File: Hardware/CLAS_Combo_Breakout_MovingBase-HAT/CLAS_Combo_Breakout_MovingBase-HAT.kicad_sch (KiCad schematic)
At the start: 86 parts, among them J1 USB_C_Receptacle_USB2.0, J2 ZED, J3 NEO, J4 USB_C_Receptacle_USB2.0, J5 Conn_Coaxial, Q1 DSS20200, U1 USBLC6-2P6, U2 ZED-F9P, U3 NEO-D9C-00B, U4 USBLC6-2P6, U5 NJU77251F, U6 AP2112K-3.3, U7 NT1191GEAE3S, U8 F2933NBGP, U9 PD0922J5050S2HF

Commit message: ISP4520周辺回路を設計中
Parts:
- removed ANT1: GGBLA.125.A, GGBLA.125.A:GGBLA.125.A, symbol GGBLA.125.A:GGBLA.125.A
- removed BT1: MS421R, Battery_extlib:MS421R, symbol Device:Battery_Cell
- removed C1, C10, C5, C6: 1u, Capacitor_SMD:C_0603_1608Metric, symbol Device:C_Small
- removed C11, C14: 47p, Capacitor_SMD:C_0402_1005Metric, symbol Device:C_Small
- removed C12: 1000p, Capacitor_SMD:C_0603_1608Metric, symbol Device:C_Small
- removed C13: 3.9p, Capacitor_SMD:C_0402_1005Metric, symbol Device:C_Small
- removed C15, C2, C3, C4: 0.1u, Capacitor_SMD:C_0603_1608Metric, symbol Device:C_Small
- removed C16: 1.2p, Capacitor_SMD:C_0402_1005Metric, symbol Device:C_Small
- removed C9: DNF, Capacitor_SMD:C_0402_1005Metric, symbol Device:C_Small
- removed D10: PESD0402-140, Diode_SMD:D_0402_1005Metric, symbol Device:D_TVS
- removed D3: EXTANT, LED_SMD:LED_0603_1608Metric, symbol Device:LED_Small
- removed D7: CUHS20S30, CUHS20S30:CUHS20S30, symbol Device:D_Schottky_Small
- removed D8: BAS19, Package_TO_SOT_SMD:SOT-23, symbol Diode:BAS19
- removed D9: BAT54W, Package_TO_SOT_SMD:SOT-23, symbol Diode:BAT54W
- removed J4: USB_C_Receptacle_USB2.0, Connector_USB_extlib:USB_C_Receptacle_5077CR-16-SMC2-BK-TR, symbol Connector:USB_C_Receptacle_USB2.0
- removed J5: Conn_Coaxial, Connector_Coaxial_extlib:0734152063, symbol Connector:Conn_Coaxial
- removed L1: LQW18ANR12G8ZD, LQW18ANR12G8ZD:LQW18ANR12G8ZD, symbol Device:L_Small
- removed L2: LQW15AN9N5G00D, LQW15AN9N5G00D:LQW15AN9N5G00D, symbol Device:L_Small
- removed Q1: DSS20200, Package_TO_SOT_SMD:SOT-23, symbol DSS20200L-7:DSS20200L-7
- removed R1, R11, R12, R2, R3, R4, R5, R6, R7: 33, Resistor_SMD:R_0603_1608Metric, symbol Device:R_Small
- removed R10, R13, R14, R16: 27, Resistor_SMD:R_0603_1608Metric, symbol Device:R_Small
- removed R15, R17: 5.1k, Resistor_SMD:R_0603_1608Metric, symbol Device:R_Small
- removed R20: 1k, Resistor_SMD:R_0603_1608Metric, symbol Device:R_Small
- removed R24: 68, Resistor_SMD:R_0402_1005Metric, symbol Device:R_Small
- removed R25: 3, Resistor_SMD:R_0603_1608Metric, symbol Device:R_Small
- removed R26: 22k, Resistor_SMD:R_0402_1005Metric, symbol Device:R_Small
- removed R27: 3.3k, Resistor_SMD:R_0603_1608Metric, symbol Device:R_Small
- removed R28: 1.5k, Resistor_SMD:R_0402_1005Metric, symbol Device:R_Small
- removed R29, R30: 100, Resistor_SMD:R_0402_1005Metric, symbol Device:R_Small
- removed R31, R33, R34: 0, Resistor_SMD:R_0402_1005Metric, symbol Device:R_Small
- removed R32: DNF, Resistor_SMD:R_0402_1005Metric, symbol Device:R_Small
- removed TP1: SAFEBOOT_ZED, TestPoint:TestPoint_Pad_D1.0mm, symbol Connector:TestPoint
- removed TP2: SAFEBOOT_NEO, TestPoint:TestPoint_Pad_D1.0mm, symbol Connector:TestPoint
- removed U2: ZED-F9P, RF_GPS:ublox_ZED, symbol RF_GPS:ZED-F9P
- removed U3: NEO-D9C-00B, NEO-D9:NEO-D9, symbol NEO-D9:NEO-D9C-00B
- removed U4: USBLC6-2P6, Package_TO_SOT_SMD:SOT-666, symbol Power_Protection:USBLC6-2P6
- removed U5: NJU77251F, Package_TO_SOT_SMD:SOT-23-5, symbol Comparator:LMV331
- removed U7: NT1191GEAE3S, NT1191GEAE3S:NT1191GEAE3S, symbol NT1191GEAE3S:NT1191GEAE3S
- removed U8: F2933NBGP, F2933NBGP:F2933NBGP, symbol F2933NBGP:F2933NBGP
- removed U9: PD0922J5050S2HF, PD0922J5050S2HF:PD0922J5050S2HF_ANA, symbol PD0922J5050S2HF:PD0922J5050S2HF
- added C?: 1u, symbol Device:C_Small
- added C? (x2): 0.1u, symbol Device:C_Small
- added D?: CUHS20S30, CUHS20S30:CUHS20S30, symbol Device:D_Schottky_Small
- added R?: 10k, symbol Device:R_Small
- added SW?: SW_Push, symbol Switch:SW_Push
- added U?: ISP4520-AS, symbol ISP4520-AS:ISP4520-AS
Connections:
- net +3.3V: now also C?.1, C?.1, D?.1 (K), R?.1, U?.15 (VDD)
- net GND: now also C?.2, C?.2, SW?.2, U?.1 (GND), U?.14 (GND), U?.21 (GND), U?.22 (GND), U?.23 (GND), U?.26 (GND), U?.27 (GND), U?.28 (GND), U?.29 (GND), U?.30 (GND), U?.31 (GND), U?.32 (GND), U?.33 (GND), U?.36 (GND), U?.74 (GND)
- net RESET: now also C?.2, D?.2 (A), R?.2, SW?.1, U?.40 (P0_21/RESET)
- net SCL: now also U?.5 (P0_07)
- net SDA: now also U?.2 (P0_12)
- new net: U?.24 (LORA_TR), U?.25 (LORA_ANT)
- new net: U?.34 (BLE_ANT), U?.35 (BLE_TR)
- new net: U?.45 (NC), U?.46 (NC), U?.47 (NC), U?.48 (NC), U?.49 (NC), U?.50 (NC), U?.51 (NC), U?.52 (NC), U?.53 (NC), U?.54 (NC), U?.55 (NC), U?.56 (NC), U?.57 (NC), U?.58 (NC), U?.59 (NC), U?.60 (NC), U?.61 (NC), U?.62 (NC), U?.63 (NC), U?.64 (NC), U?.65 (NC), U?.66 (NC), U?.67 (NC), U?.68 (NC), U?.69 (NC), U?.70 (NC), U?.71 (NC), U?.72 (NC), U?.73 (NC)
- new net DTR: C?.1
- new net RXIN: U?.8 (P0_08)
- new net SWDCLK: U?.37 (SWDCLK)
- new net SWDIO: U?.38 (SWDIO)
- new net TXOUT: U?.10 (P0_06)
- no-connect marks 17 -> 4
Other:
- note added: "AUTO RESET"
- note added: "Battery Control"
- note added: "CPU"
- note added: "Low freq属性でないピンをsoftwareserialにしてデバッグに使う"
- note added: "UARTは1chまで 割り当てはデフォルトのまま USBとF9Pで共有"
- note added: "variant.hを編集して、ISP4520のデータシートの設計例で使われている SCL:P0_07 SDA:P0_12 に変更（元のピンは内部でSX1261とのSPIで使われている）"
- note removed: "3.29V"
- note removed: "9.5nH"
- note removed: "Auto antenna select"
- note removed: "Backup Battery"
- note removed: "External active antenna detect"
- note removed: "Indicator"
- note removed: "Initial Charge: 3.0-3.3V Charge Rate: 1mA MAX Voff: 2.0V"
- note removed: "Omit damping resistor"
- note removed: "PullUp"
- note removed: "Push-Pull Output"
- note removed: "RF Amplifiers"
- note removed: "RF Receiver"
- note removed: "Voltage Regulation"
- note removed: "ZED-F9P_NEO-D9C_Combo"
- note removed: "detection current:3mA"
- note removed: "アンテナが接続されていないとLOW 接続されるとHI"
- company: (none) -> U.E.C.wings
- title: (none) -> CLAS_Combo_Breakout_MovingBase-HAT
- moved on the sheet: C7, C8, D1, D2, D4, D5, D6, H1, H2, H3, H4, J2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

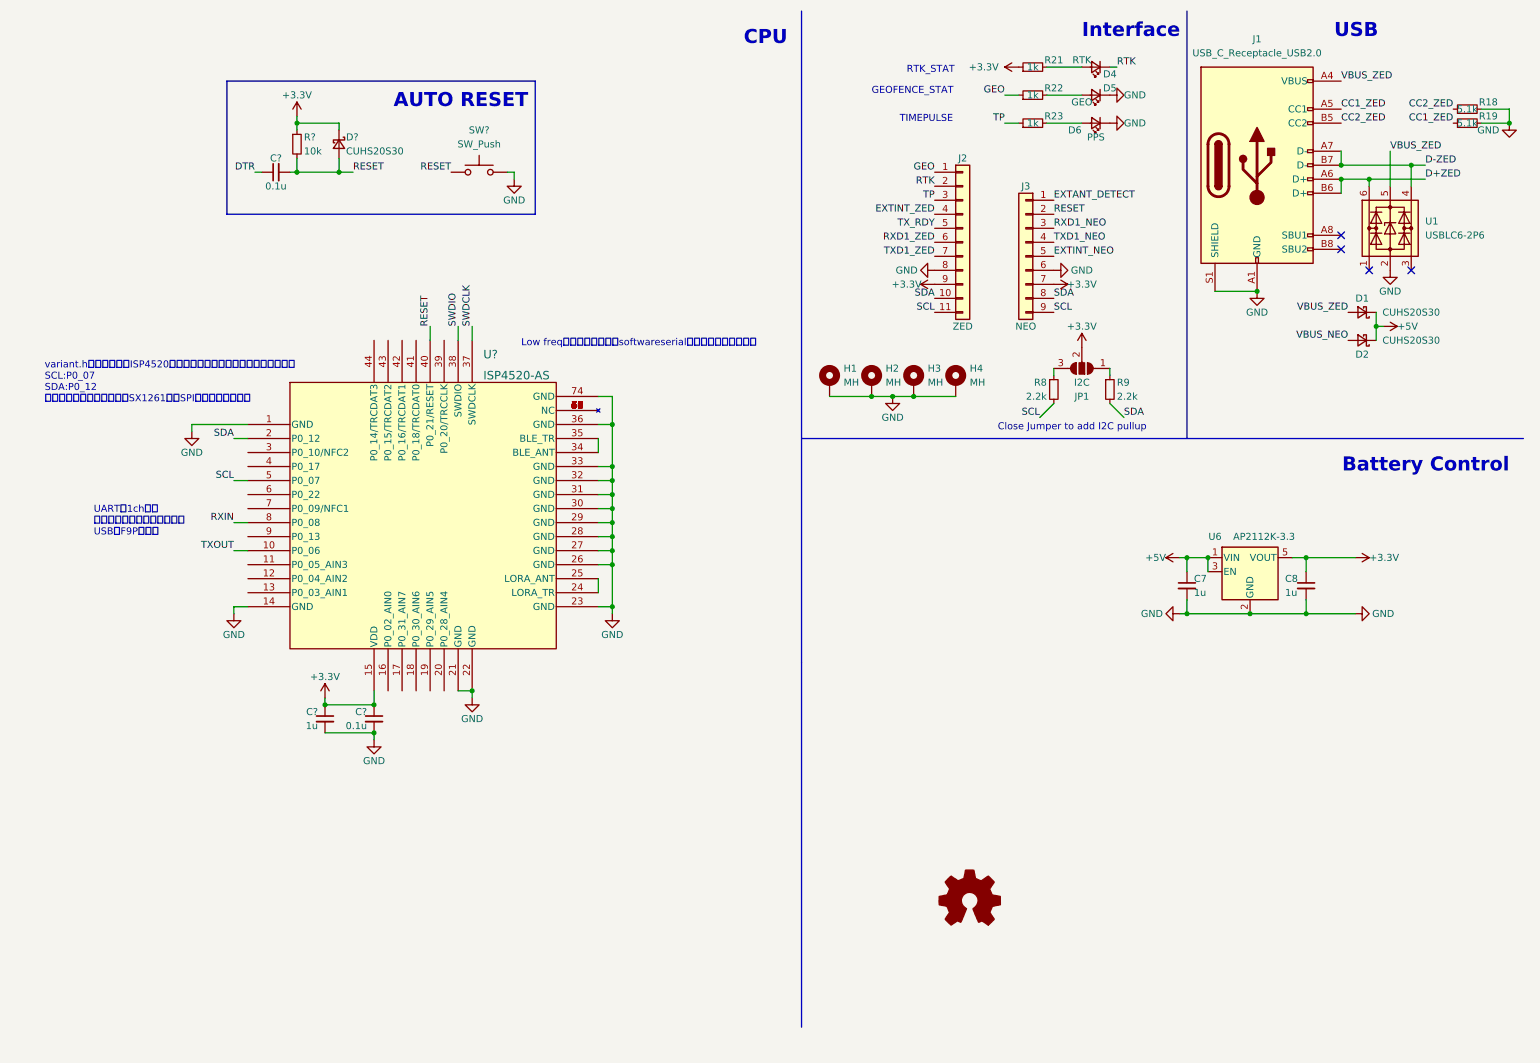
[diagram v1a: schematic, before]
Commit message: 電源回路描いた
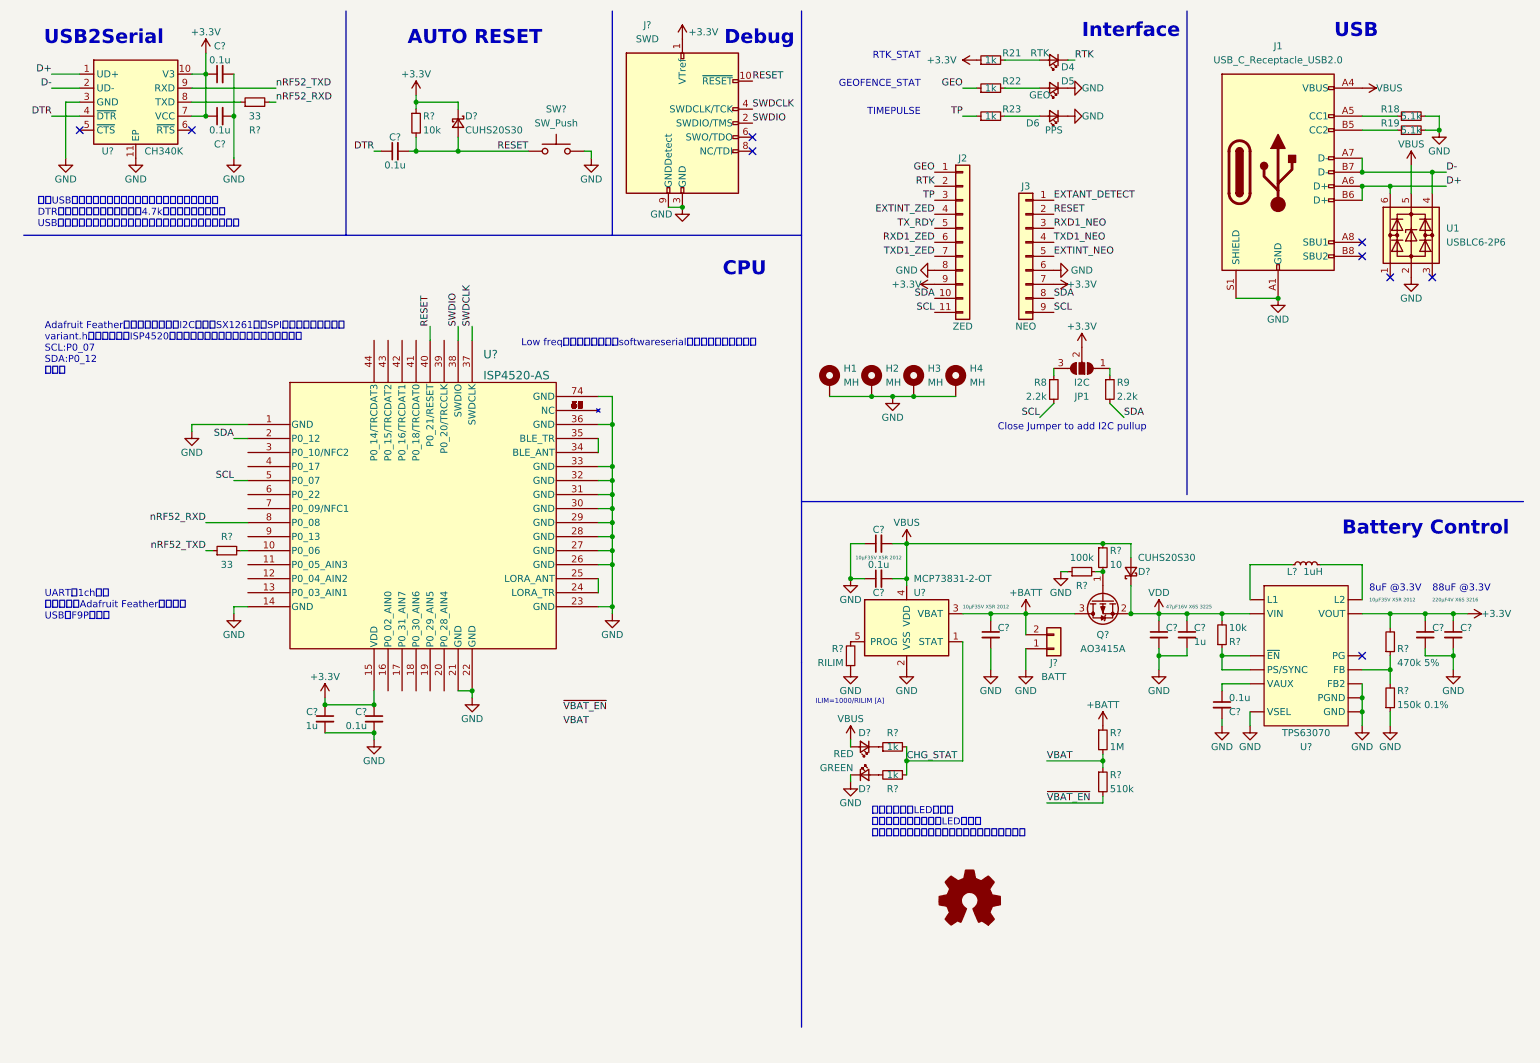
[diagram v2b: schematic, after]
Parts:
- removed C7, C8: 1u, Capacitor_SMD:C_0603_1608Metric, symbol Device:C_Small
- removed D1, D2: CUHS20S30, CUHS20S30:CUHS20S30, symbol Device:D_Schottky_Small
- removed U6: AP2112K-3.3, Package_TO_SOT_SMD:SOT-23-5, symbol Regulator_Linear:AP2112K-3.3
- added C? (x3): 10μF35V X5R 2012, Capacitor_SMD:C_0805_2012Metric, symbol Device:C_Small
- added C?: 47μF16V X6S 3225, Capacitor_SMD:C_1210_3225Metric, symbol Device:C_Small
- added C?: 0.1u, Capacitor_SMD:C_0603_1608Metric, symbol Device:C_Small
- added C? (x3): 0.1u, symbol Device:C_Small
- added C?: 1u, Capacitor_SMD:C_0603_1608Metric, symbol Device:C_Small
- added C?: 220μF4V X6S 3216, Capacitor_SMD:C_1206_3216Metric, symbol Device:C_Small
- added D?: CUHS20S30, CUHS20S30:CUHS20S30, symbol Device:D_Schottky_Small
- added D?: GREEN, LED_SMD:LED_0603_1608Metric, symbol Device:LED_Small
- added D?: RED, LED_SMD:LED_0603_1608Metric, symbol Device:LED_Small
- added J?: BATT, symbol Connector_Generic:Conn_01x02
- added J?: SWD, symbol Connector:Conn_ARM_JTAG_SWD_10
- added L?: 1uH, Inductor_SMD:L_1210_3225Metric, symbol Device:L_Small
- added Q?: AO3415A, symbol Device:Q_PMOS_GSD
- added R?: 510k, symbol Device:R_Small
- added R?: 150k 0.1%, Resistor_SMD:R_0603_1608Metric, symbol Device:R_Small
- added R? (x2): 33, symbol Device:R_Small
- added R?: 100k, Resistor_SMD:R_0603_1608Metric, symbol Device:R_Small
- added R?: 1M, symbol Device:R_Small
- added R?: RILIM, symbol Device:R_Small
- added R?: 10, symbol Device:R_Small
- added R? (x2): 1k, Resistor_SMD:R_0603_1608Metric, symbol Device:R_Small
- added R?: 470k 5%, Resistor_SMD:R_0603_1608Metric, symbol Device:R_Small
- added R?: 10k, Resistor_SMD:R_0603_1608Metric, symbol Device:R_Small
- added U?: CH340K, symbol Interface_USB_extlib:CH340K
- added U?: MCP73831-2-OT, Package_TO_SOT_SMD:SOT-23-5, symbol Battery_Management:MCP73831-2-OT
- added U?: TPS63070, Module_SparkFun_Buck-Boost:VQFN-15-HR(3X2.5), symbol Module_SparkFun_Buck-Boost:TPS63070
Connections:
- net +3.3V: now also C?.1, C?.1, C?.1, C?.1, J?.1 (VTref), R?.2, U?.10 (V3), U?.7 (VCC), U?.P$7/8 (VOUT)
- net DTR: now also U?.4 (~{DTR})
- net GND: now also C?.1, C?.1, C?.2, C?.2, C?.2, C?.2, C?.2, C?.2, C?.2, C?.2, D?.1 (K), J?.1 (Pin_1), J?.3 (GND), J?.5 (GND), J?.9 (GNDDetect), R?.1, R?.1, R?.1, U?.11 (EP), U?.2 (VSS), U?.3 (GND), U?.P$10 (PGND), U?.P$15 (VSEL), U?.P$4 (GND), U?.P$6 (FB2)
- net RESET: now also J?.10 (~{RESET})
- net SWDCLK: now also J?.4 (SWDCLK/TCK)
- net SWDIO: now also J?.2 (SWDIO/TMS)
- net CC1_ZED: no longer names the net of R19.1
- net CC1_ZED: now also J1.B5 (CC2); no longer J1.A5 (CC1)
- net CC2_ZED: no longer names the net of R18.1
- net CC2_ZED: now also J1.A5 (CC1); no longer J1.B5 (CC2)
- net D+ZED renamed D+
- net D+: now also U?.1 (UD+)
- net D-ZED renamed D-
- net D-: now also U?.2 (UD-)
- net RXIN renamed nRF52_RXD
- net nRF52_RXD: now also R?.2
- net TXOUT: no longer names the net of U?.10 (P0_06)
- net TXOUT: now also R?.2
- net VBUS_ZED renamed VBUS
- net VBUS: now also C?.2, C?.2, D?.2 (A), D?.2 (A), R?.1, U?.4 (VDD)
- new net: R?.1, R?.2, U?.P$5 (FB)
- new net: R?.1, U?.8 (TXD)
- new net: Q?.1 (G), R?.2, R?.2
- new net: R?.2, U?.5 (PROG)
- new net: C?.1, U?.P$3 (VAUX)
- new net: D?.1 (K), R?.1
- new net: L?.1, U?.P$11 (L1)
- new net: L?.2, U?.P$9 (L2)
- new net: D?.2 (A), R?.2
- new net: R?.1, U?.P$1 (PS/SYNC), U?.P$14 (~{EN})
- new net +BATT: C?.1, J?.2 (Pin_2), Q?.3 (D), R?.1, U?.3 (VBAT)
- new net CHG_STAT: R?.1, R?.2, U?.1 (STAT)
- new net VBAT: R?.1, R?.2
- new net VDD: C?.1, C?.1, D?.1 (K), Q?.2 (S), R?.2, U?.P$12/13 (VIN)
- new net nRF52_TXD: R?.1, U?.9 (RXD)
- new net ~{VBAT_EN}: R?.2
- no-connect marks 4 -> 9
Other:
- note added: "88uF @3.3V"
- note added: "8uF @3.3V"
- note added: "Adafruit Featherで指定されているI2CピンはSX1261とのSPIで使われているため variant.hを編集して、ISP4520のデータシートの設計例で指定されている SCL:P0_07 SDA:P0_12 に変更"
- note added: "Debug"
- note added: "ILIM=1000/RILIM [A]"
- note added: "UARTは1chまで 割り当てはAdafruit Featherに従った USBとF9Pで共有"
- note added: "USB2Serial"
- note added: "充電中は赤色LEDが点灯 充電が完了すると緑色LEDが点灯 シャットダウンまたはバッテリ未接続で両方点灯"
- note added: "差動USBのダンピング抵抗はデータシートには無かった DTRはプッシュプル出力だが、4.7kでプルダウンすると USBコンフィギュレーションを外部から設定することができる"
- note removed: "UARTは1chまで 割り当てはデフォルトのまま USBとF9Pで共有"
- note removed: "variant.hを編集して、ISP4520のデータシートの設計例で使われている SCL:P0_07 SDA:P0_12 に変更（元のピンは内部でSX1261とのSPIで使われている）"
- moved on the sheet: C?, D4, D5, D6, D?, J1, R18, R19, R21, R22, R23, R?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

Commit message: カイロズカッコカリ
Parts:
- removed C? (x3): 10μF35V X5R 2012, Capacitor_SMD:C_0805_2012Metric, symbol Device:C_Small
- removed C?: 47μF16V X6S 3225, Capacitor_SMD:C_1210_3225Metric, symbol Device:C_Small
- removed C?: 0.1u, Capacitor_SMD:C_0603_1608Metric, symbol Device:C_Small
- removed C?: 1u, Capacitor_SMD:C_0603_1608Metric, symbol Device:C_Small
- removed C?: 220μF4V X6S 3216, Capacitor_SMD:C_1206_3216Metric, symbol Device:C_Small
- removed L?: 1uH, Inductor_SMD:L_1210_3225Metric, symbol Device:L_Small
- removed R?: 150k 0.1%, Resistor_SMD:R_0603_1608Metric, symbol Device:R_Small
- removed R?: 470k 5%, Resistor_SMD:R_0603_1608Metric, symbol Device:R_Small
- removed R?: 10k, Resistor_SMD:R_0603_1608Metric, symbol Device:R_Small
- removed U?: TPS63070, Module_SparkFun_Buck-Boost:VQFN-15-HR(3X2.5), symbol Module_SparkFun_Buck-Boost:TPS63070
- added C? (x2): 47μF6.3V X5R 1608, symbol Device:C_Small
- added C?: 0.1u, symbol Device:C_Small
- added C?: 220μF4V X6S 3216, Capacitor_SMD:C_1206_3216Metric, symbol Device:C_Small
- added C?: 2200pF50V CH 1608, Capacitor_SMD:C_0603_1608Metric, symbol Device:C_Small
- added C?: 100μF10V X5R 3216, Capacitor_SMD:C_1206_3216Metric, symbol Device:C_Small
- added J?: SMA, symbol Connector:Conn_Coaxial
- added J?: MMCX, symbol Connector:Conn_Coaxial
- added R?: Rtop, symbol Device:R_Small
- added R?: Rbtm, symbol Device:R_Small
- added R?: 26.2k, Resistor_SMD:R_0603_1608Metric, symbol Device:R_Small
- added R?: 10k, symbol Device:R_Small
- added SW?: SW_SPDT, symbol Switch:SW_SPDT
- added U?: TMUX136, symbol Analog_Switch_extlib:TMUX136
- added U?: LTM4693, symbol LTM4693:LTM4693
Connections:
- net +3.3V: now also C?.1, C?.2, U?.10 (VCC), U?.C5 (VOUT), U?.D4 (VOUT), U?.D5 (VOUT)
- net +BATT: now also C?.1
- net GND: now also C?.1, C?.1, C?.2, C?.2, C?.2, C?.2, J?.2 (Ext), J?.2 (Ext), R?.2, R?.2, SW?.3 (C), U?.5 (GND), U?.6 (~{EN}), U?.A1 (GND), U?.A3 (GND), U?.A5 (GND), U?.B1 (GND), U?.B3 (GND), U?.B5 (GND), U?.C3 (GND)
- net RESET: no longer J3.2 (Pin_2)
- net RXD1_ZED: now also U?.3 (B1)
- net TXD1_ZED: now also U?.4 (B2)
- net VBUS: now also C?.2
- net VDD: now also C?.1, R?.1, U?.C1 (VIN), U?.D1 (VIN), U?.D2 (VIN), U?.D3 (SS), U?.E2 (MODE/SYNC)
- net nRF52_RXD: now also U?.7 (COM2); no longer R?.2
- net nRF52_TXD: now also U?.8 (COM1); no longer U?.9 (RXD)
- net CHG_STAT renamed ~{CHG_STAT}
- new net: R?.2, SW?.1 (A)
- new net: U?.A2 (SW1), U?.B2 (SW1), U?.C2 (SW1)
- new net: U?.A4 (SW2), U?.B4 (SW2), U?.C4 (SW2)
- new net: R?.1, SW?.2 (B), U?.E1 (RUN/UVLO)
- new net: R?.1, U?.E4 (FB)
- new net: R?.1, U?.E5 (COMP)
- new net: J?.1 (In), J?.1 (In)
- new net: C?.1, R?.2
- new net CH340K_RXD: U?.1 (A1), U?.9 (RXD)
- new net CH340K_TXD: R?.2, U?.2 (A2)
- new net RESET_ZED_NEO: J3.2 (Pin_2)
- new net ZED_UART_EN: U?.9 (SEL)
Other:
- note added: "3.300V @26.26k"
- note added: "3.314V @26.1k"
- note added: "33uF @5V"
- note added: "42uF @4.2V"
- note added: "9.4uF @5V"
- note added: "BurstModeは-1%程度の出力電圧リップルが発生するため使わない"
- note added: "CHG_STATはアナログピンに接続しユニバーサル領域にも引き出す"
- note added: "GNSSの各種ピンも繋げる"
- note added: "I2Cピンは2セットあるから配線しやすい方を使う"
- note added: "RF"
- note added: "SDA,SCLは下ボードでプルアップ"
- note added: "SEL ---- X Low High"
- note added: "SELとENは内部でLowにプルダウンされてる ->デフォルトでAが有効"
- note added: "TXはダンピング抵抗内臓"
- note added: "UART MUX"
- note added: "| -------- | Disable | COM to A | COM to B"
- note added: "| EN ----- | High | Low | Low"
- note added: "スイッチOFF時にUVLOを設定する抵抗に電流が流れない"
- note added: "スイッチングDCDCの近くに UARTを通さないようにする"
- note added: "充電中は赤色LEDが点灯 充電が完了すると緑色LEDが点灯 シャットダウンまたはバッテリ未接続で両方点灯 そのときCHG_STATは2.5Vになるはず"
- note removed: "8uF @3.3V"
- note removed: "充電中は赤色LEDが点灯 充電が完了すると緑色LEDが点灯 シャットダウンまたはバッテリ未接続で両方点灯"
- moved on the sheet: C?, D?, J?, Q?, R?, SW?, U?
